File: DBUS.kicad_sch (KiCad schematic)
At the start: 5 parts

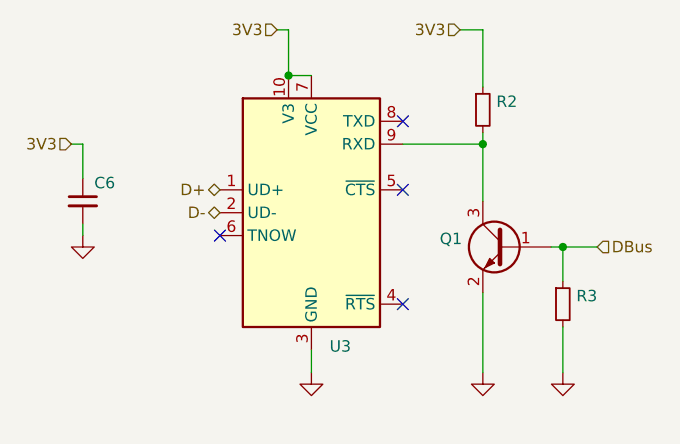
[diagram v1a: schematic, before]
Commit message: Change '5V' tag to '+5V' net
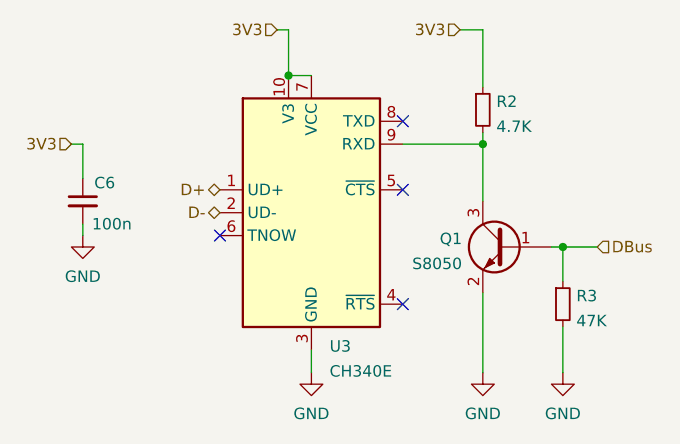
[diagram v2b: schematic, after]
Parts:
- C6: value (none) -> 100n; footprint (none) -> Capacitor_SMD:C_0603_1608Metric
- Q1: value (none) -> S8050; footprint (none) -> Package_TO_SOT_SMD:SOT-23
- R2: value (none) -> 4.7K; footprint (none) -> Resistor_SMD:R_0603_1608Metric
- R3: value (none) -> 47K; footprint (none) -> Resistor_SMD:R_0603_1608Metric
- U3: value (none) -> CH340E; footprint (none) -> Package_SO:MSOP-10_3x3mm_P0.5mm
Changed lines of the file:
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@@
       (effects (font (size 1.27 1.27)) (justify right))
     )
-    (property "Value" "" (id 1) (at 108.966 90.17 0)
+    (property "Value" "100n" (id 1) (at 108.966 90.17 0)
       (effects (font (size 1.27 1.27)) (justify right))
     )
-    (property "Footprint" "" (id 2) (at 107.95 87.63 0)
+    (property "Footprint" "Capacitor_SMD:C_0603_1608Metric" (id 2) (at 107.95 87.63 0)
       (effects (font (size 1.27 1.27)) hide)
     )
@@
       (effects (font (size 1.27 1.27)) hide)
     )
-    (property "Value" "" (id 1) (at 161.29 111.2425 0))
+    (property "Value" "GND" (id 1) (at 161.29 111.2425 0))
     (property "Footprint" "" (id 2) (at 161.29 106.68 0)
       (effects (font (size 1.27 1.27)) hide)
@@
       (effects (font (size 1.27 1.27)) (justify left))
     )
-    (property "Value" "" (id 1) (at 153.8986 79.3366 0)
+    (property "Value" "4.7K" (id 1) (at 153.8986 79.3366 0)
       (effects (font (size 1.27 1.27)) (justify left))
     )
-    (property "Footprint" "" (id 2) (at 152.4 77.47 0)
+    (property "Footprint" "Resistor_SMD:R_0603_1608Metric" (id 2) (at 152.4 77.47 0)
       (effects (font (size 1.27 1.27)) hide)
     )
@@
       (effects (font (size 1.27 1.27)) (justify left))
     )
-    (property "Value" "" (id 1) (at 135.3694 106.5246 0)
+    (property "Value" "CH340E" (id 1) (at 135.3694 106.5246 0)
       (effects (font (size 1.27 1.27)) (justify left))
     )
-    (property "Footprint" "" (id 2) (at 134.62 102.87 0)
+    (property "Footprint" "Package_SO:MSOP-10_3x3mm_P0.5mm" (id 2) (at 134.62 102.87 0)
       (effects (font (size 1.27 1.27)) (justify left) hide)
     )
@@
       (effects (font (size 1.27 1.27)) (justify left))
     )
-    (property "Value" "" (id 1) (at 162.7886 100.9266 0)
+    (property "Value" "47K" (id 1) (at 162.7886 100.9266 0)
       (effects (font (size 1.27 1.27)) (justify left))
     )
-    (property "Footprint" "" (id 2) (at 161.29 99.06 0)
+    (property "Footprint" "Resistor_SMD:R_0603_1608Metric" (id 2) (at 161.29 99.06 0)
       (effects (font (size 1.27 1.27)) hide)
     )
@@
       (effects (font (size 1.27 1.27)) hide)
     )
-    (property "Value" "" (id 1) (at 133.35 111.2425 0))
+    (property "Value" "GND" (id 1) (at 133.35 111.2425 0))
     (property "Footprint" "" (id 2) (at 133.35 106.68 0)
       (effects (font (size 1.27 1.27)) hide)
@@
       (effects (font (size 1.27 1.27)) hide)
     )
-    (property "Value" "" (id 1) (at 107.95 96.0025 0))
+    (property "Value" "GND" (id 1) (at 107.95 96.0025 0))
     (property "Footprint" "" (id 2) (at 107.95 91.44 0)
       (effects (font (size 1.27 1.27)) hide)
@@
       (effects (font (size 1.27 1.27)) (justify left))
     )
-    (property "Value" "" (id 1) (at 150.0886 94.5766 0)
+    (property "Value" "S8050" (id 1) (at 150.0886 94.5766 0)
       (effects (font (size 1.27 1.27)) (justify left))
     )
-    (property "Footprint" "" (id 2) (at 149.86 90.17 0)
+    (property "Footprint" "Package_TO_SOT_SMD:SOT-23" (id 2) (at 149.86 90.17 0)
       (effects (font (size 1.27 1.27)) hide)
     )
@@
       (effects (font (size 1.27 1.27)) hide)
     )
-    (property "Value" "" (id 1) (at 152.4 111.2425 0))
+    (property "Value" "GND" (id 1) (at 152.4 111.2425 0))
     (property "Footprint" "" (id 2) (at 152.4 106.68 0)
       (effects (font (size 1.27 1.27)) hide)

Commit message: Change the map and rebuild the PCB
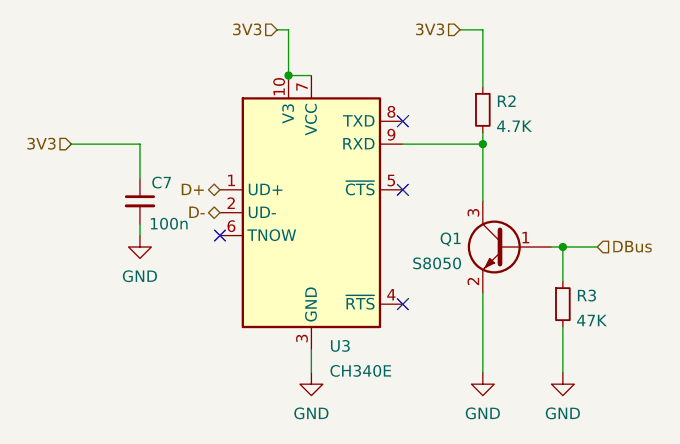
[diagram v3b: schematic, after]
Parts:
- removed C6: 100n, Capacitor_SMD:C_0603_1608Metric, symbol Device:C_Small
- added C7: 100n, Capacitor_SMD:C_0603_1608Metric, symbol Device:C_Small
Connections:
- net 3V3: now also C7.1
- net GND: now also C7.2
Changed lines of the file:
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@@
-    (stroke (width 0) (type default) (color 0 0 0 0))
-  )
-  (wire (pts (xy 107.95 81.28) (xy 107.95 85.09))
     (stroke (width 0) (type default) (color 0 0 0 0))
   )
@@
     (stroke (width 0) (type default) (color 0 0 0 0))
   )
+  (wire (pts (xy 114.3 81.28) (xy 114.3 85.09))
+    (stroke (width 0) (type default) (color 0 0 0 0))
+  )
   (wire (pts (xy 133.35 104.14) (xy 133.35 106.68))
     (stroke (width 0) (type default) (color 0 0 0 0))
   )
-  (wire (pts (xy 106.68 81.28) (xy 107.95 81.28))
+  (wire (pts (xy 106.68 81.28) (xy 114.3 81.28))
+    (stroke (width 0) (type default) (color 0 0 0 0))
+  )
+  (wire (pts (xy 114.3 90.17) (xy 114.3 91.44))
     (stroke (width 0) (type default) (color 0 0 0 0))
   )
   (wire (pts (xy 152.4 81.28) (xy 152.4 87.63))
-    (stroke (width 0) (type default) (color 0 0 0 0))
-  )
-  (wire (pts (xy 107.95 90.17) (xy 107.95 91.44))
     (stroke (width 0) (type default) (color 0 0 0 0))
   )
@@
     (effects (font (size 1.27 1.27)) (justify right))
   )
-  (symbol (lib_id "Device:C_Small") (at 107.95 87.63 0) (mirror y) (unit 1)
-    (in_bom yes) (on_board yes)
-    (property "Reference" "C6" (id 0) (at 109.22 85.598 0)
-      (effects (font (size 1.27 1.27)) (justify right))
-    )
-    (property "Value" "100n" (id 1) (at 108.966 90.17 0)
-      (effects (font (size 1.27 1.27)) (justify right))
-    )
-    (property "Footprint" "Capacitor_SMD:C_0603_1608Metric" (id 2) (at 107.95 87.63 0)
-      (effects (font (size 1.27 1.27)) hide)
-    )
-    (property "Datasheet" "~" (id 3) (at 107.95 87.63 0)
-      (effects (font (size 1.27 1.27)) hide)
-    )
-    (pin "1")
-    (pin "2")
-  )
   (symbol (lib_id "power:GND") (at 161.29 106.68 0) (unit 1)
     (in_bom yes) (on_board yes) (fields_autoplaced)
@@
     )
     (property "Datasheet" "" (id 3) (at 161.29 106.68 0)
+      (effects (font (size 1.27 1.27)) hide)
+    )
+    (pin "1")
+  )
+  (symbol (lib_id "power:GND") (at 114.3 91.44 0) (unit 1)
+    (in_bom yes) (on_board yes) (fields_autoplaced)
+    (property "Reference" "#PWR0117" (id 0) (at 114.3 97.79 0)
+      (effects (font (size 1.27 1.27)) hide)
+    )
+    (property "Value" "GND" (id 1) (at 114.3 96.0025 0))
+    (property "Footprint" "" (id 2) (at 114.3 91.44 0)
+      (effects (font (size 1.27 1.27)) hide)
+    )
+    (property "Datasheet" "" (id 3) (at 114.3 91.44 0)
       (effects (font (size 1.27 1.27)) hide)
     )
@@
     (pin "1")
   )
-  (symbol (lib_id "power:GND") (at 107.95 91.44 0) (unit 1)
-    (in_bom yes) (on_board yes) (fields_autoplaced)
-    (property "Reference" "#PWR0117" (id 0) (at 107.95 97.79 0)
+  (symbol (lib_id "Device:C_Small") (at 114.3 87.63 0) (mirror y) (unit 1)
+    (in_bom yes) (on_board yes)
+    (property "Reference" "C7" (id 0) (at 115.57 85.598 0)
+      (effects (font (size 1.27 1.27)) (justify right))
+    )
+    (property "Value" "100n" (id 1) (at 115.316 90.17 0)
+      (effects (font (size 1.27 1.27)) (justify right))
+    )
+    (property "Footprint" "Capacitor_SMD:C_0603_1608Metric" (id 2) (at 114.3 87.63 0)
       (effects (font (size 1.27 1.27)) hide)
     )
-    (property "Value" "GND" (id 1) (at 107.95 96.0025 0))
-    (property "Footprint" "" (id 2) (at 107.95 91.44 0)
-      (effects (font (size 1.27 1.27)) hide)
-    )
-    (property "Datasheet" "" (id 3) (at 107.95 91.44 0)
+    (property "Datasheet" "~" (id 3) (at 114.3 87.63 0)
       (effects (font (size 1.27 1.27)) hide)
     )
     (pin "1")
+    (pin "2")
   )
   (symbol (lib_id "Device:Q_NPN_BEC") (at 154.94 92.71 0) (mirror y) (unit 1)
